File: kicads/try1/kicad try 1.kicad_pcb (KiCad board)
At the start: 2 copper layers, 35 parts, among them P2 GND, P3 CONN_01X08, P4 A2 A3 A4 A5 A6, P5 Mutual, P6 CONN_01X08, SW1 SW_PUSH, SW2 SW_PUSH, SW3 SW_PUSH, SW4 SW_PUSH, U2 CD74HCT4067, U3 CD74HCT4067

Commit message: forward with the pcb design
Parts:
- moved U2 139.8 mm to (169.0, 141.0)
- moved U3 137.4 mm to (169.0, 64.0)
- moved D11 25.6 mm to (140.0, 77.5)
- moved D3 22.9 mm to (90.0, 77.5)
- moved D7 22.9 mm to (115.0, 77.5)
- moved D15 21.6 mm to (165.0, 77.5)
- moved D9 21.4 mm to (140.0, 130.0)
- moved D1 21.2 mm to (90.0, 130.0)
- moved D13 21.2 mm to (165.0, 130.0)
- moved D5 21.2 mm to (115.0, 130.0)
- moved uP1 10.1 mm to (186.0, 151.0)
- moved SW1 8.25 mm to (179.0, 142.0)
- moved SW2 8.12 mm to (179.0, 117.0)
- moved SW4 7.92 mm to (179.0, 67.0)
- moved SW3 7.78 mm to (179.0, 92.0)
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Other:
- net class Default: clearance 0.2 -> 0.2032; trace_width 0.25 -> 0.2032; via_dia 0.6 -> 0.7493; via_drill 0.4 -> 0.50038
- net class seeed added: clearance 0.2032, trace_width 0.2032, via_dia 0.7493, via_drill 0.50038
- rule trace_clearance: 0.2 -> 0.2032
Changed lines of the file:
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@@
   (general
     (links 166)
-    (no_connects 118)
-    (area 59.460541 49.121665 231.326042 162.267166)
+    (no_connects 166)
+    (area 59.036499 47.536499 230.502834 160.282)
     (thickness 1.6)
     (drawings 0)
@@
   (page A4)
   (layers
-    (0 F.Cu signal hide)
-    (31 B.Cu signal hide)
+    (0 F.Cu signal)
+    (31 B.Cu signal)
     (32 B.Adhes user)
     (33 F.Adhes user)
@@
   )
   (setup
-    (last_trace_width 0.25)
-    (trace_clearance 0.2)
+    (last_trace_width 0.2032)
+    (trace_clearance 0.2032)
     (zone_clearance 0.508)
     (zone_45_only no)
@@
     (segment_width 0.2)
     (edge_width 0.1)
-    (via_size 0.6)
-    (via_drill 0.4)
+    (via_size 0.7493)
+    (via_drill 0.50038)
     (via_min_size 0.4)
     (via_min_drill 0.3)
@@
     (pad_to_mask_clearance 0)
     (aux_axis_origin 0 0)
-    (visible_elements 7FFFEFFF)
+    (visible_elements 7FFFFFFF)
     (pcbplotparams
       (layerselection 0x00030_80000001)
@@
   (net 106 "Net-(PAD-matrix-4-PadSIG3)")
   (net_class Default "This is the default net class."
-    (clearance 0.2)
-    (trace_width 0.25)
-    (via_dia 0.6)
-    (via_drill 0.4)
+    (clearance 0.2032)
+    (trace_width 0.2032)
+    (via_dia 0.7493)
+    (via_drill 0.50038)
     (uvia_dia 0.3)
     (uvia_drill 0.1)
@@
     (add_net "Net-(uP1-Pad9)")
   )
+  (net_class seeed ""
+    (clearance 0.2032)
+    (trace_width 0.2032)
+    (via_dia 0.7493)
+    (via_drill 0.50038)
+    (uvia_dia 0.3)
+    (uvia_drill 0.1)
+  )
   (module Diodes_ThroughHole:Diode_DO-41_SOD81_Horizontal_RM10 (layer F.Cu)
-    (at 90.664042 151.182626 180)
+    (at 90 130 180)
     (descr "Diode, DO-41, SOD81, Horizontal, RM 10mm,")
     (tags "Diode, DO-41, SOD81, Horizontal, RM 10mm, 1N4007, SB140,")
@@
   )
   (module Diodes_ThroughHole:Diode_DO-41_SOD81_Horizontal_RM10 (layer F.Cu)
-    (at 90.664042 128.322626 180)
+    (at 90 125 180)
     (descr "Diode, DO-41, SOD81, Horizontal, RM 10mm,")
     (tags "Diode, DO-41, SOD81, Horizontal, RM 10mm, 1N4007, SB140,")
@@
   )
   (module Diodes_ThroughHole:Diode_DO-41_SOD81_Horizontal_RM10 (layer F.Cu)
-    (at 90.664042 100.382626 180)
+    (at 90 77.5 180)
     (descr "Diode, DO-41, SOD81, Horizontal, RM 10mm,")
     (tags "Diode, DO-41, SOD81, Horizontal, RM 10mm, 1N4007, SB140,")
@@
   )
   (module Diodes_ThroughHole:Diode_DO-41_SOD81_Horizontal_RM10 (layer F.Cu)
-    (at 90.664042 74.982626 180)
+    (at 90 72.5 180)
     (descr "Diode, DO-41, SOD81, Horizontal, RM 10mm,")
     (tags "Diode, DO-41, SOD81, Horizontal, RM 10mm, 1N4007, SB140,")
@@
   )
   (module Diodes_ThroughHole:Diode_DO-41_SOD81_Horizontal_RM10 (layer F.Cu)
-    (at 114.794042 151.182626 180)
+    (at 115 130 180)
     (descr "Diode, DO-41, SOD81, Horizontal, RM 10mm,")
     (tags "Diode, DO-41, SOD81, Horizontal, RM 10mm, 1N4007, SB140,")
@@
   )
   (module Diodes_ThroughHole:Diode_DO-41_SOD81_Horizontal_RM10 (layer F.Cu)
-    (at 114.794042 125.782626 180)
+    (at 115 125 180)
     (descr "Diode, DO-41, SOD81, Horizontal, RM 10mm,")
     (tags "Diode, DO-41, SOD81, Horizontal, RM 10mm, 1N4007, SB140,")
@@
   )
   (module Diodes_ThroughHole:Diode_DO-41_SOD81_Horizontal_RM10 (layer F.Cu)
-    (at 114.794042 100.382626 180)
+    (at 115 77.5 180)
     (descr "Diode, DO-41, SOD81, Horizontal, RM 10mm,")
     (tags "Diode, DO-41, SOD81, Horizontal, RM 10mm, 1N4007, SB140,")
@@
   )
   (module Diodes_ThroughHole:Diode_DO-41_SOD81_Horizontal_RM10 (layer F.Cu)
-    (at 114.385102 74.982626 180)
+    (at 115 72.5 180)
     (descr "Diode, DO-41, SOD81, Horizontal, RM 10mm,")
     (tags "Diode, DO-41, SOD81, Horizontal, RM 10mm, 1N4007, SB140,")
@@
   )
   (module Diodes_ThroughHole:Diode_DO-41_SOD81_Horizontal_RM10 (layer F.Cu)
-    (at 142.734042 151.185166 180)
+    (at 140 130 180)
     (descr "Diode, DO-41, SOD81, Horizontal, RM 10mm,")
     (tags "Diode, DO-41, SOD81, Horizontal, RM 10mm, 1N4007, SB140,")
@@
   )
   (module Diodes_ThroughHole:Diode_DO-41_SOD81_Horizontal_RM10 (layer F.Cu)
-    (at 142.734042 124.515166 180)
+    (at 140 125 180)
     (descr "Diode, DO-41, SOD81, Horizontal, RM 10mm,")
     (tags "Diode, DO-41, SOD81, Horizontal, RM 10mm, 1N4007, SB140,")
@@
   )
   (module Diodes_ThroughHole:Diode_DO-41_SOD81_Horizontal_RM10 (layer F.Cu)
-    (at 142.734042 102.922626 180)
+    (at 140 77.5 180)
     (descr "Diode, DO-41, SOD81, Horizontal, RM 10mm,")
     (tags "Diode, DO-41, SOD81, Horizontal, RM 10mm, 1N4007, SB140,")
@@
   )
   (module Diodes_ThroughHole:Diode_DO-41_SOD81_Horizontal_RM10 (layer F.Cu)
-    (at 142.734042 76.252626 180)
+    (at 140 72.5 180)
     (descr "Diode, DO-41, SOD81, Horizontal, RM 10mm,")
     (tags "Diode, DO-41, SOD81, Horizontal, RM 10mm, 1N4007, SB140,")
@@
   )
   (module Diodes_ThroughHole:Diode_DO-41_SOD81_Horizontal_RM10 (layer F.Cu)
-    (at 165.594042 151.182626 180)
+    (at 165 130 180)
     (descr "Diode, DO-41, SOD81, Horizontal, RM 10mm,")
     (tags "Diode, DO-41, SOD81, Horizontal, RM 10mm, 1N4007, SB140,")
@@
   )
   (module Diodes_ThroughHole:Diode_DO-41_SOD81_Horizontal_RM10 (layer F.Cu)
-    (at 165.594042 128.322626 180)
+    (at 165 125 180)
     (descr "Diode, DO-41, SOD81, Horizontal, RM 10mm,")
     (tags "Diode, DO-41, SOD81, Horizontal, RM 10mm, 1N4007, SB140,")
@@
   )
   (module Diodes_ThroughHole:Diode_DO-41_SOD81_Horizontal_RM10 (layer F.Cu)
-    (at 165.594042 99.112626 180)
+    (at 165 77.5 180)
     (descr "Diode, DO-41, SOD81, Horizontal, RM 10mm,")
     (tags "Diode, DO-41, SOD81, Horizontal, RM 10mm, 1N4007, SB140,")
@@
   )
   (module Diodes_ThroughHole:Diode_DO-41_SOD81_Horizontal_RM10 (layer F.Cu)
-    (at 165.594042 73.712626 180)
+    (at 165 72.5 180)
     (descr "Diode, DO-41, SOD81, Horizontal, RM 10mm,")
     (tags "Diode, DO-41, SOD81, Horizontal, RM 10mm, 1N4007, SB140,")
@@
   )
   (module button-pad-autotel:2x2-buttonpad-sparkfun-autotel (layer F.Cu)
-    (at 110.224042 153.685166 90)
+    (at 110 151.5 90)
     (fp_text reference PAD-matrix-1 (at 0 0 90) (layer F.SilkS)
       (effects (font (thickness 0.15)))
@@
   )
   (module button-pad-autotel:2x2-buttonpad-sparkfun-autotel (layer F.Cu)
-    (at 110.384042 102.885166 90)
+    (at 110 101.5 90)
     (fp_text reference PAD-matrix-2 (at 0 0 90) (layer F.SilkS)
       (effects (font (thickness 0.15)))
@@
   )
   (module button-pad-autotel:2x2-buttonpad-sparkfun-autotel (layer F.Cu)
-    (at 161.024042 153.685166 90)
+    (at 160 151.5 90)
     (fp_text reference PAD-matrix-3 (at 0 0 90) (layer F.SilkS)
       (effects (font (thickness 0.15)))
@@
   )
   (module button-pad-autotel:2x2-buttonpad-sparkfun-autotel (layer F.Cu)
-    (at 161.024042 102.885166 90)
+    (at 160 101.5 90)
     (fp_text reference PAD-matrix-4 (at 0 0 90) (layer F.SilkS)
       (effects (font (thickness 0.15)))
@@
   )
   (module Buttons_Switches_ThroughHole:SW_PUSH_6mm (layer F.Cu)
-    (at 171.254042 144.835166 90)
+    (at 179 142 90)
     (descr https://www.omron.com/ecb/products/pdf/en-b3f.pdf)
     (tags "tact sw push 6mm")
@@
   )
   (module Buttons_Switches_ThroughHole:SW_PUSH_6mm (layer F.Cu)
-    (at 171.254042 119.435166 90)
+    (at 179 117 90)
     (descr https://www.omron.com/ecb/products/pdf/en-b3f.pdf)
     (tags "tact sw push 6mm")
@@
   )
   (module Buttons_Switches_ThroughHole:SW_PUSH_6mm (layer F.Cu)
-    (at 171.254042 92.765166 90)
+    (at 179 92 90)
     (descr https://www.omron.com/ecb/products/pdf/en-b3f.pdf)
     (tags "tact sw push 6mm")
@@
   )
   (module Buttons_Switches_ThroughHole:SW_PUSH_6mm (layer F.Cu)
-    (at 171.254042 68.635166 90)
+    (at 179 67 90)
     (descr https://www.omron.com/ecb/products/pdf/en-b3f.pdf)
     (tags "tact sw push 6mm")
@@
   )
   (module SparkFun-DigitalIC:TSSOP-24 (layer F.Cu)
-    (at 31.75 114.3)
+    (at 169 141)
     (descr "<h3>24-pin TSSOP with Exposed Thermal Pad</h3>\nUsed on: <ul>\n<li>Allegro A6282 16-bit LED driver</li>\n</ul>\nLast modified: 8/21/10<br>\n<b>***Unproven***</b><br>")
     (fp_text reference U2 (at -4.17 2.01 90) (layer F.SilkS)
@@
   )
   (module SparkFun-DigitalIC:TSSOP-24 (layer F.Cu)
-    (at 31.75 71.12)
+    (at 169 64)
     (descr "<h3>24-pin TSSOP with Exposed Thermal Pad</h3>\nUsed on: <ul>\n<li>Allegro A6282 16-bit LED driver</li>\n</ul>\nLast modified: 8/21/10<br>\n<b>***Unproven***</b><br>")
     (fp_text reference U3 (at -4.17 2.01 90) (layer F.SilkS)
@@
   )
   (module ArduProMiniTKB:ArduProMini-6 (layer F.Cu)
-    (at 196.074042 149.915166 90)
+    (at 186 151 90)
     (fp_text reference uP1 (at 11.43 1.27 90) (layer F.SilkS)
       (effects (font (size 1.5 1.5) (thickness 0.15)))

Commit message: board PCB iteration prior to route
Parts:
- added ?: , SparkFun-Connectors:1X08, F.Cu at (191.8, 102.9)
- added P10: CONN_01X08, SparkFun-Connectors:1X08, F.Cu at (209.6, 87.6)
- added P11: CONN_01X08, SparkFun-Connectors:1X08, F.Cu at (226.1, 113.0)
- added P12: CONN_01X08, SparkFun-Connectors:1X08, F.Cu at (229.9, 95.2)
- added P13: CONN_01X08, SparkFun-Connectors:1X08, F.Cu at (209.6, 59.7)
- added P14: CONN_01X08, SparkFun-Connectors:1X08, F.Cu at (191.8, 55.9)
- added P15: CONN_01X08, SparkFun-Connectors:1X08, F.Cu at (229.9, 74.9)
- added P16: CONN_01X08, SparkFun-Connectors:1X08, F.Cu at (226.1, 92.7)
- added P17: CONN_01X08, SparkFun-Connectors:1X08, F.Cu at (209.6, 74.9)
- added P18: CONN_01X08, SparkFun-Connectors:1X08, F.Cu at (191.8, 78.7)
- added P7: CONN_01X08, SparkFun-Connectors:1X08, F.Cu at (218.4, 95.2)
- added P8: CONN_01X08, SparkFun-Connectors:1X08, F.Cu at (214.6, 113.0)
- added P9: CONN_01X08, SparkFun-Connectors:1X08, F.Cu at (191.8, 83.8)
- ?: renamed from VCC; value CONN_01X08 -> (none)
- ?: renamed from P2; value GND -> (none)
- A0 pulldown: renamed from R2
- A1 pulldown: renamed from R1
- P5: value Mutual -> CONN_01X08
- PB5: renamed from P3; value CONN_01X08 -> (none)
- U2, U3: moved to B.Cu
- ~: renamed from P4; value A2 A3 A4 A5 A6 -> (none)
- moved U2 92.7 mm to (85.1, 101.6)
- moved U3 50.9 mm to (134.6, 101.6)
- moved ? 37.6 mm to (209.6, 108.0)
- moved P6 22.7 mm to (214.6, 92.7), turned to 90 degrees
- moved A1 pulldown 10.6 mm to (207.5, 130.0)
- moved A0 pulldown 9.66 mm to (211.0, 119.8)
- moved P5 8.97 mm to (218.4, 74.9), turned to 270 degrees
- moved PB5 8.03 mm to (209.6, 113.0)
- moved ? 8.03 mm to (209.6, 92.7)
- moved ~ 8.01 mm to (191.8, 97.8)
- moved SW1 6.44 mm to (172.6, 142.3)
- moved SW2 6.44 mm to (172.6, 117.3)
- moved SW3 6.44 mm to (172.6, 92.3)
- moved SW4 6.44 mm to (172.6, 67.3)
- moved uP1 0.59 mm to (185.4, 151.1)
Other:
- board outline added: 172.5 x 100 mm
- board text added: "PB5...PB0"

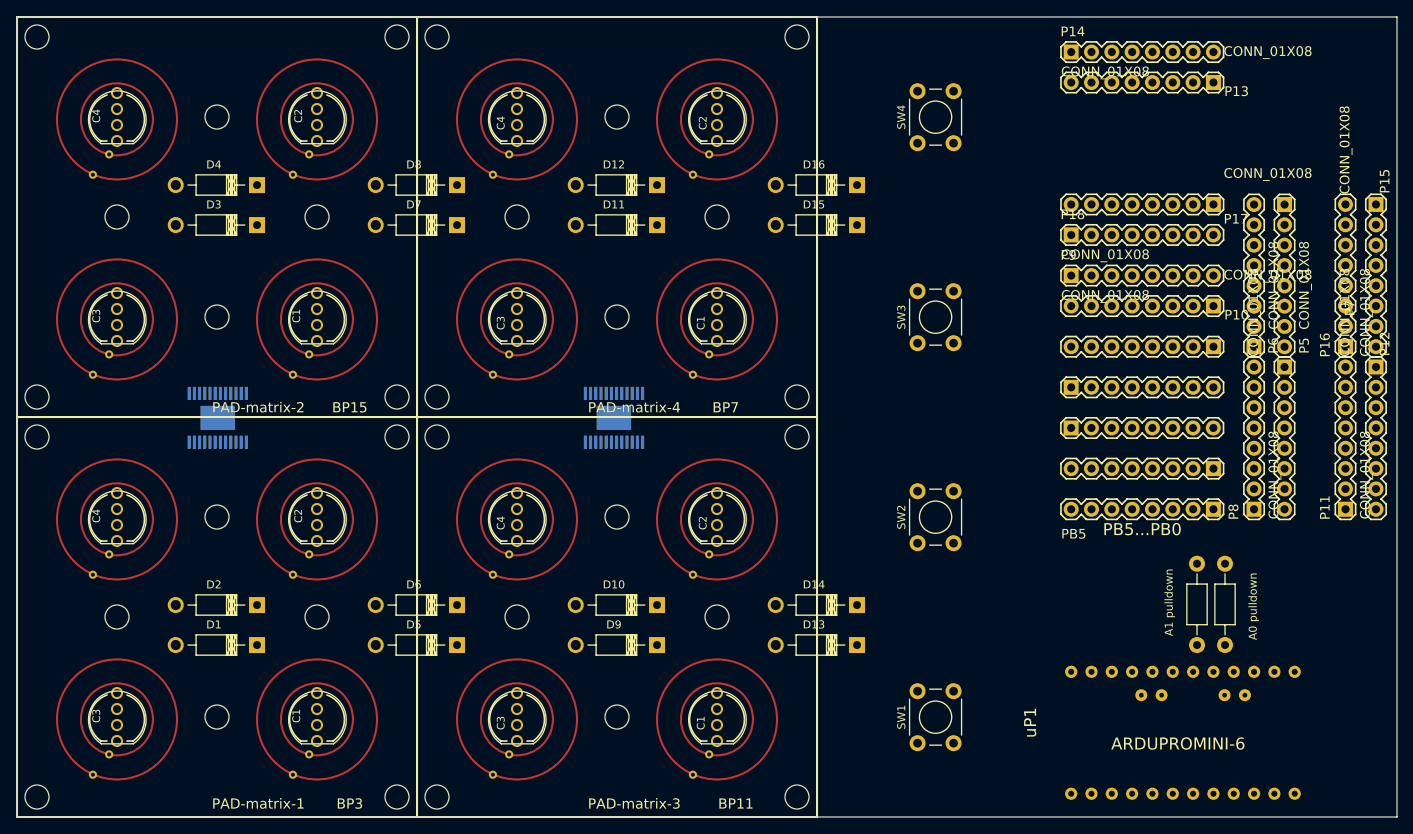
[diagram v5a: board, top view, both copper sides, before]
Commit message: fix big mistake on schematic
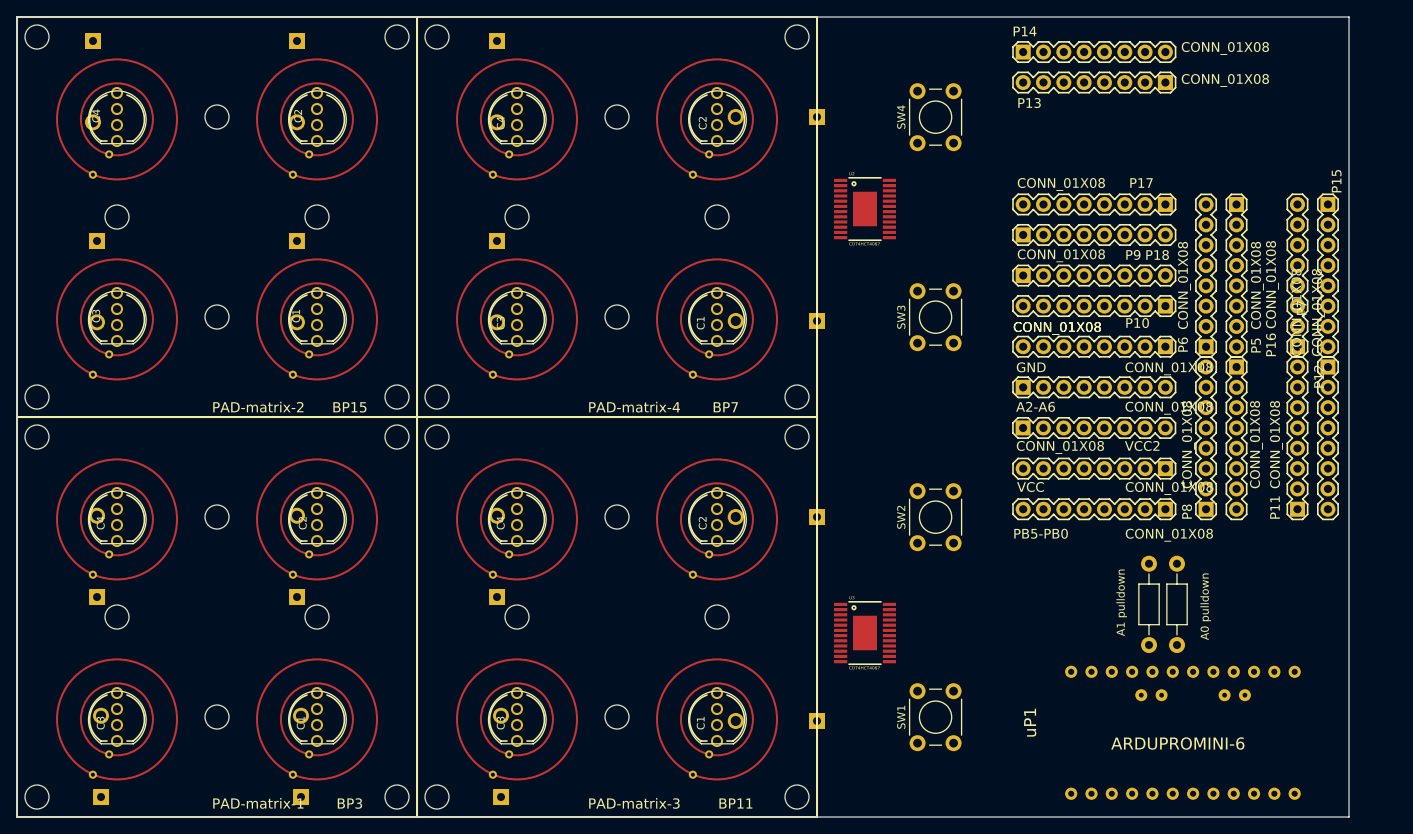
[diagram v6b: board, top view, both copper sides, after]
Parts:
- A2-A6: renamed from ~; value (none) -> CONN_01X08
- CONN_01X08: renamed from ?; value (none) -> VCC2
- D1, D10, D11, D12, D13, D14, D15, D16, D2, D3, D4, D5, D6, D7, D8, D9: moved to B.Cu
- GND, VCC: renamed from ?; value (none) -> CONN_01X08
- PB5-PB0: renamed from PB5; value (none) -> CONN_01X08
- U2, U3: moved to F.Cu
- moved U2 85.0 mm to (166.0, 75.5), turned to 270 degrees
- moved U3 41.3 mm to (166.0, 128.5), turned to 270 degrees
- moved D4 27.3 mm to (69.5, 54.5), turned to 270 degrees
- moved D5 27.2 mm to (95.5, 149.0), turned to 90 degrees
- moved D1 27.2 mm to (70.5, 149.0), turned to 90 degrees
- moved D9 27.2 mm to (120.5, 149.0), turned to 90 degrees
- moved D12 26.9 mm to (120.0, 54.5), turned to 270 degrees
- moved D8 26.9 mm to (95.0, 54.5), turned to 270 degrees
- moved D7 20.1 mm to (95.0, 79.5), turned to 270 degrees
- moved D11 20.1 mm to (120.0, 79.5), turned to 270 degrees
- moved D3 20.1 mm to (70.0, 79.5), turned to 270 degrees
- moved D10 20.0 mm to (120.0, 124.0), turned to 90 degrees
- moved D6 20.0 mm to (95.0, 124.0), turned to 90 degrees
- moved D2 20.0 mm to (70.0, 124.0), turned to 90 degrees
- moved D15 13.0 mm to (160.0, 89.5)
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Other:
- board size 172.5 x 100 mm -> 166.5 x 100 mm
- board text removed: "PB5...PB0"
